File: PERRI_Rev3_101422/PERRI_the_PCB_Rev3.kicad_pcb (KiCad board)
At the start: 2 copper layers, 163 x 100 mm, 101 parts, among them J1 Conn_01x03, J2 Conn_01x03, J3 Conn_01x03, J4 302-R101, J5 Conn_01x02, Q1 MMST3904-7-F, SW1 SW_DIP_x08, U1 TPS2595, U2 NCV8508, U3 PCA9554ADB, U4 TMP441AIDCNR

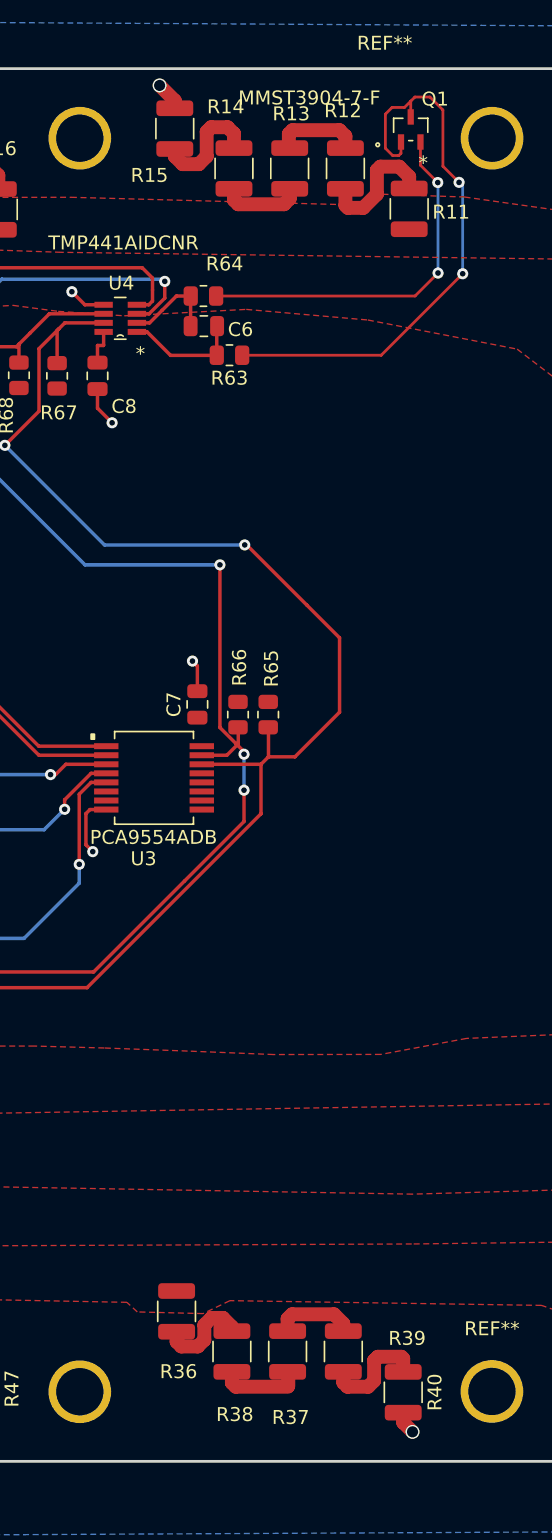
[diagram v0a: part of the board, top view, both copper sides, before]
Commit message: Fixed transistor issue. Review completed. -Dennis H. Calderon
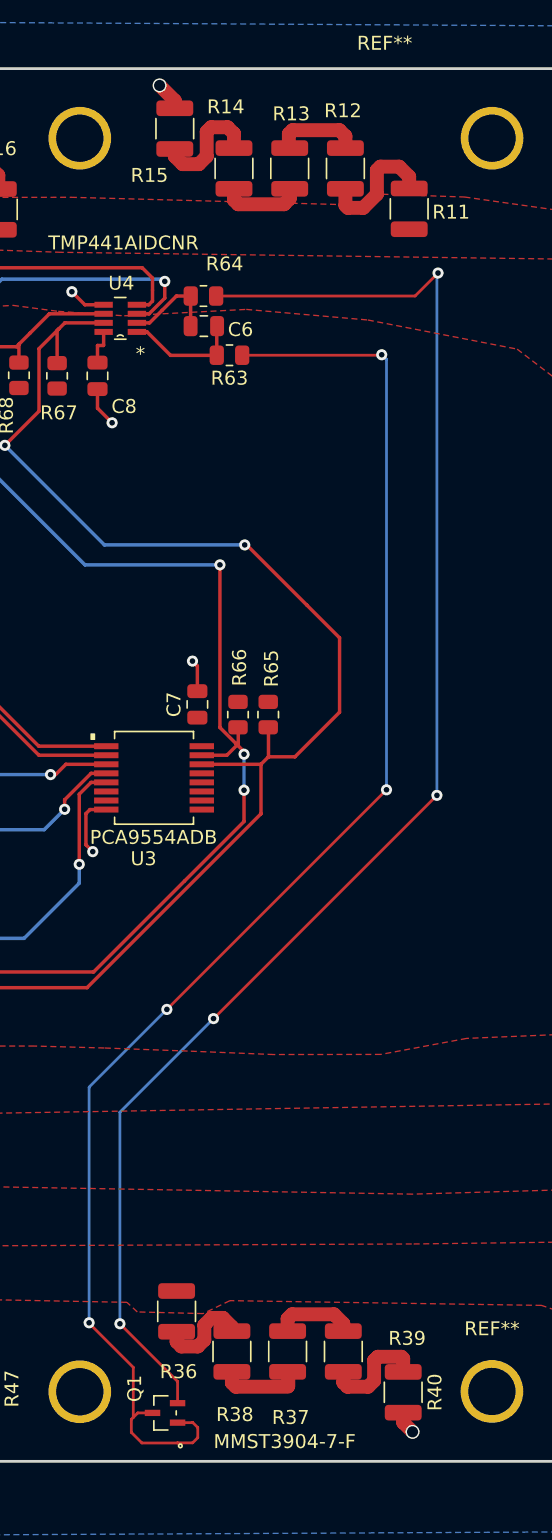
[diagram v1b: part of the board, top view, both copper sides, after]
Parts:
- moved Q1 93.8 mm to (159.7, 142.8), turned to 90 degrees
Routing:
- net /DXN: track 26.5 -> 108.9 mm, vias 2 -> 4
- net /DXP: track 41.4 -> 106.9 mm, vias 2 -> 4
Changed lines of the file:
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@@
   )
   (footprint "MMST3904-7-F:MMST3904-7-F" (layer "F.Cu")
-    (at 177.339999 50.599999)
+    (at 159.7 142.75 90)
     (property "Sheetfile" "PERRI_the_PCB_Rev3.kicad_sch")
     (property "Sheetname" "")
     (attr through_hole)
-    (fp_text reference "Q1" (at 1.75 -2.18 180) (layer "F.SilkS")
+    (fp_text reference "Q1" (at 1.75 -2.18 90) (layer "F.SilkS")
       (effects (font (size 1 1) (thickness 0.15)))
     )
-    (fp_text value "MMST3904-7-F" (at -7.28 -2.26 180) (layer "F.SilkS")
+    (fp_text value "MMST3904-7-F" (at -2.06 8.59 180) (layer "F.SilkS")
       (effects (font (size 1 1) (thickness 0.15)))
     )
-    (fp_text user "*" (at 0.9 2.41) (layer "F.SilkS")
-      (effects (font (size 1 1) (thickness 0.15)))
-    )
-    (fp_text user "Copyright 2021 Accelerated Designs. All rights reserved." (at 0 0) (layer "Cmts.User")
+    (fp_text user "Copyright 2021 Accelerated Designs. All rights reserved." (at 0 0 90) (layer "Cmts.User")
       (effects (font (size 0.127 0.127) (thickness 0.002)))
     )
-    (fp_text user "*" (at 0 0) (layer "F.Fab")
+    (fp_text user "*" (at 0 0 90) (layer "F.Fab")
       (effects (font (size 1 1) (thickness 0.15)))
     )
@@
     (fp_line (start 0.5 1.1) (end 0.9 1.1) (layer "F.Fab") (width 0.1))
     (fp_circle (center -0.846 0.421) (end -0.719 0.421) (layer "F.Fab") (width 0.1) (fill none))
-    (pad "1" smd rect (at -0.700001 0.900001) (size 0.4508 1.1112) (layers "F.Cu" "F.Paste" "F.Mask")
+    (pad "1" smd rect (at -0.700001 0.900001 90) (size 0.4508 1.1112) (layers "F.Cu" "F.Paste" "F.Mask")
       (net 7 "/DXP") (pinfunction "E") (pintype "passive"))
-    (pad "2" smd rect (at 0.700001 0.900001) (size 0.4508 1.1112) (layers "F.Cu" "F.Paste" "F.Mask")
+    (pad "2" smd rect (at 0.700001 0.900001 90) (size 0.4508 1.1112) (layers "F.Cu" "F.Paste" "F.Mask")
       (net 6 "/DXN") (pinfunction "B") (pintype "passive"))
-    (pad "3" smd rect (at 0 -0.9) (size 0.4508 1.1112) (layers "F.Cu" "F.Paste" "F.Mask")
+    (pad "3" smd rect (at 0 -0.9 90) (size 0.4508 1.1112) (layers "F.Cu" "F.Paste" "F.Mask")
       (net 7 "/DXP") (pinfunction "C") (pintype "passive"))
   )
@@
   (segment (start 154.85 66.12) (end 154.85 67.34) (width 0.25) (layer "F.Cu") (net 5))
   (segment (start 154.86 66.11) (end 154.85 66.12) (width 0.25) (layer "F.Cu") (net 5))
-  (segment (start 179.28 54.41) (end 178.04 53.17) (width 0.2) (layer "F.Cu") (net 6))
+  (segment (start 163.18 114.44) (end 163.19 114.44) (width 0.2) (layer "F.Cu") (net 6))
+  (segment (start 160.600001 142.049999) (end 160.600001 140.490001) (width 0.2) (layer "F.Cu") (net 6))
   (segment (start 163.36875 62.56) (end 177.65 62.56) (width 0.2) (layer "F.Cu") (net 6))
   (segment (start 177.65 62.56) (end 179.3 60.91) (width 0.2) (layer "F.Cu") (net 6))
-  (segment (start 178.04 53.17) (end 178.04 51.5) (width 0.2) (layer "F.Cu") (net 6))
+  (segment (start 163.19 114.44) (end 179.22 98.41) (width 0.2) (layer "F.Cu") (net 6))
+  (segment (start 160.600001 140.490001) (end 156.46 136.35) (width 0.2) (layer "F.Cu") (net 6))
+  (via (at 179.22 98.41) (size 0.8) (drill 0.4) (layers "F.Cu" "B.Cu") (net 6))
+  (via (at 156.46 136.35) (size 0.8) (drill 0.4) (layers "F.Cu" "B.Cu") (net 6))
   (via (at 179.3 60.91) (size 0.8) (drill 0.4) (layers "F.Cu" "B.Cu") (net 6))
-  (via (at 179.28 54.41) (size 0.8) (drill 0.4) (layers "F.Cu" "B.Cu") (net 6))
-  (segment (start 179.3 60.91) (end 179.3 54.43) (width 0.2) (layer "B.Cu") (net 6))
-  (segment (start 179.3 54.43) (end 179.28 54.41) (width 0.2) (layer "B.Cu") (net 6))
+  (via (at 163.18 114.44) (size 0.8) (drill 0.4) (layers "F.Cu" "B.Cu") (net 6))
+  (segment (start 163.18 114.44) (end 156.46 121.16) (width 0.2) (layer "B.Cu") (net 6))
+  (segment (start 179.22 60.99) (end 179.3 60.91) (width 0.2) (layer "B.Cu") (net 6))
+  (segment (start 156.46 121.16) (end 156.46 136.35) (width 0.2) (layer "B.Cu") (net 6))
+  (segment (start 179.22 98.41) (end 179.22 60.99) (width 0.2) (layer "B.Cu") (net 6))
   (segment (start 165.23875 66.81) (end 175.22 66.81) (width 0.2) (layer "F.Cu") (net 7))
-  (segment (start 176.04048 52.47048) (end 176.48 52.47048) (width 0.2) (layer "F.Cu") (net 7))
-  (segment (start 179.65 53.24) (end 179.65 49.2) (width 0.2) (layer "F.Cu") (net 7))
-  (segment (start 177.64 48.27) (end 177.339999 48.570001) (width 0.2) (layer "F.Cu") (net 7))
-  (segment (start 177.339999 48.570001) (end 177.339999 49.699999) (width 0.2) (layer "F.Cu") (net 7))
-  (segment (start 180.81 54.4) (end 179.65 53.24) (width 0.2) (layer "F.Cu") (net 7))
-  (segment (start 176 49.02) (end 175.52 49.5) (width 0.2) (layer "F.Cu") (net 7))
-  (segment (start 175.22 66.81) (end 181.07 60.96) (width 0.2) (layer "F.Cu") (net 7))
-  (segment (start 178.72 48.27) (end 177.64 48.27) (width 0.2) (layer "F.Cu") (net 7))
-  (segment (start 175.52 51.95) (end 176.04048 52.47048) (width 0.2) (layer "F.Cu") (net 7))
-  (segment (start 176.48 52.47048) (end 176.639998 52.310482) (width 0.2) (layer "F.Cu") (net 7))
-  (segment (start 175.52 49.5) (end 175.52 51.95) (width 0.2) (layer "F.Cu") (net 7))
-  (segment (start 177.339999 48.570001) (end 176.89 49.02) (width 0.2) (layer "F.Cu") (net 7))
-  (segment (start 176.89 49.02) (end 176 49.02) (width 0.2) (layer "F.Cu") (net 7))
-  (segment (start 176.639998 52.310482) (end 176.639998 51.5) (width 0.2) (layer "F.Cu") (net 7))
-  (segment (start 179.65 49.2) (end 178.72 48.27) (width 0.2) (layer "F.Cu") (net 7))
-  (via (at 180.81 54.4) (size 0.8) (drill 0.4) (layers "F.Cu" "B.Cu") (net 7))
-  (via (at 181.07 60.96) (size 0.8) (drill 0.4) (layers "F.Cu" "B.Cu") (net 7))
-  (segment (start 181.07 54.66) (end 180.81 54.4) (width 0.2) (layer "B.Cu") (net 7))
-  (segment (start 181.07 60.96) (end 181.07 54.66) (width 0.2) (layer "B.Cu") (net 7))
+  (segment (start 162.05 143.8) (end 161.68 143.43) (width 0.2) (layer "F.Cu") (net 7))
+  (segment (start 157.42 143.07) (end 157.42 139.48) (width 0.2) (layer "F.Cu") (net 7))
+  (segment (start 158.8 142.75) (end 157.74 142.75) (width 0.2) (layer "F.Cu") (net 7))
+  (segment (start 161.659999 143.450001) (end 160.600001 143.450001) (width 0.2) (layer "F.Cu") (net 7))
+  (segment (start 157.28 144.15) (end 158.04 144.91) (width 0.2) (layer "F.Cu") (net 7))
+  (segment (start 157.28 143.21) (end 157.28 144.15) (width 0.2) (layer "F.Cu") (net 7))
+  (segment (start 162.05 144.53) (end 162.05 143.8) (width 0.2) (layer "F.Cu") (net 7))
+  (segment (start 160.600001 144.899999) (end 161.680001 144.899999) (width 0.2) (layer "F.Cu") (net 7))
+  (segment (start 159.83 113.78) (end 175.6 98.01) (width 0.2) (layer "F.Cu") (net 7))
+  (segment (start 175.22 66.81) (end 175.255 66.775) (width 0.2) (layer "F.Cu") (net 7))
+  (segment (start 157.42 139.48) (end 154.25 136.31) (width 0.2) (layer "F.Cu") (net 7))
+  (segment (start 157.42 143.07) (end 157.28 143.21) (width 0.2) (layer "F.Cu") (net 7))
+  (segment (start 161.68 143.43) (end 161.659999 143.450001) (width 0.2) (layer "F.Cu") (net 7))
+  (segment (start 161.680001 144.899999) (end 162.05 144.53) (width 0.2) (layer "F.Cu") (net 7))
+  (segment (start 157.74 142.75) (end 157.42 143.07) (width 0.2) (layer "F.Cu") (net 7))
+  (segment (start 160.59 144.91) (end 160.600001 144.899999) (width 0.2) (layer "F.Cu") (net 7))
+  (segment (start 158.04 144.91) (end 160.59 144.91) (width 0.2) (layer "F.Cu") (net 7))
+  (segment (start 154.25 136.31) (end 154.25 136.28) (width 0.2) (layer "F.Cu") (net 7))
+  (via (at 175.255 66.775) (size 0.8) (drill 0.4) (layers "F.Cu" "B.Cu") (net 7))
+  (via (at 175.6 98.01) (size 0.8) (drill 0.4) (layers "F.Cu" "B.Cu") (net 7))
+  (via (at 154.25 136.28) (size 0.8) (drill 0.4) (layers "F.Cu" "B.Cu") (net 7))
+  (via (at 159.83 113.78) (size 0.8) (drill 0.4) (layers "F.Cu" "B.Cu") (net 7))
+  (segment (start 154.25 136.28) (end 154.25 119.36) (width 0.2) (layer "B.Cu") (net 7))
+  (segment (start 175.6 98.01) (end 175.6 67.1) (width 0.2) (layer "B.Cu") (net 7))
+  (segment (start 175.6 67.1) (end 175.27 66.77) (width 0.2) (layer "B.Cu") (net 7))
+  (segment (start 154.25 119.36) (end 159.83 113.78) (width 0.2) (layer "B.Cu") (net 7))
   (segment (start 209.45 101.6002) (end 209.45 99.99) (width 0.25) (layer "F.Cu") (net 8))
   (segment (start 216.787818 104.907818) (end 219.24 104.907818) (width 0.25) (layer "F.Cu") (net 8))
